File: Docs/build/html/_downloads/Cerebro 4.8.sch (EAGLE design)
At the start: 29 parts, among them IC1 OPA237N, T1 FJX3904TF

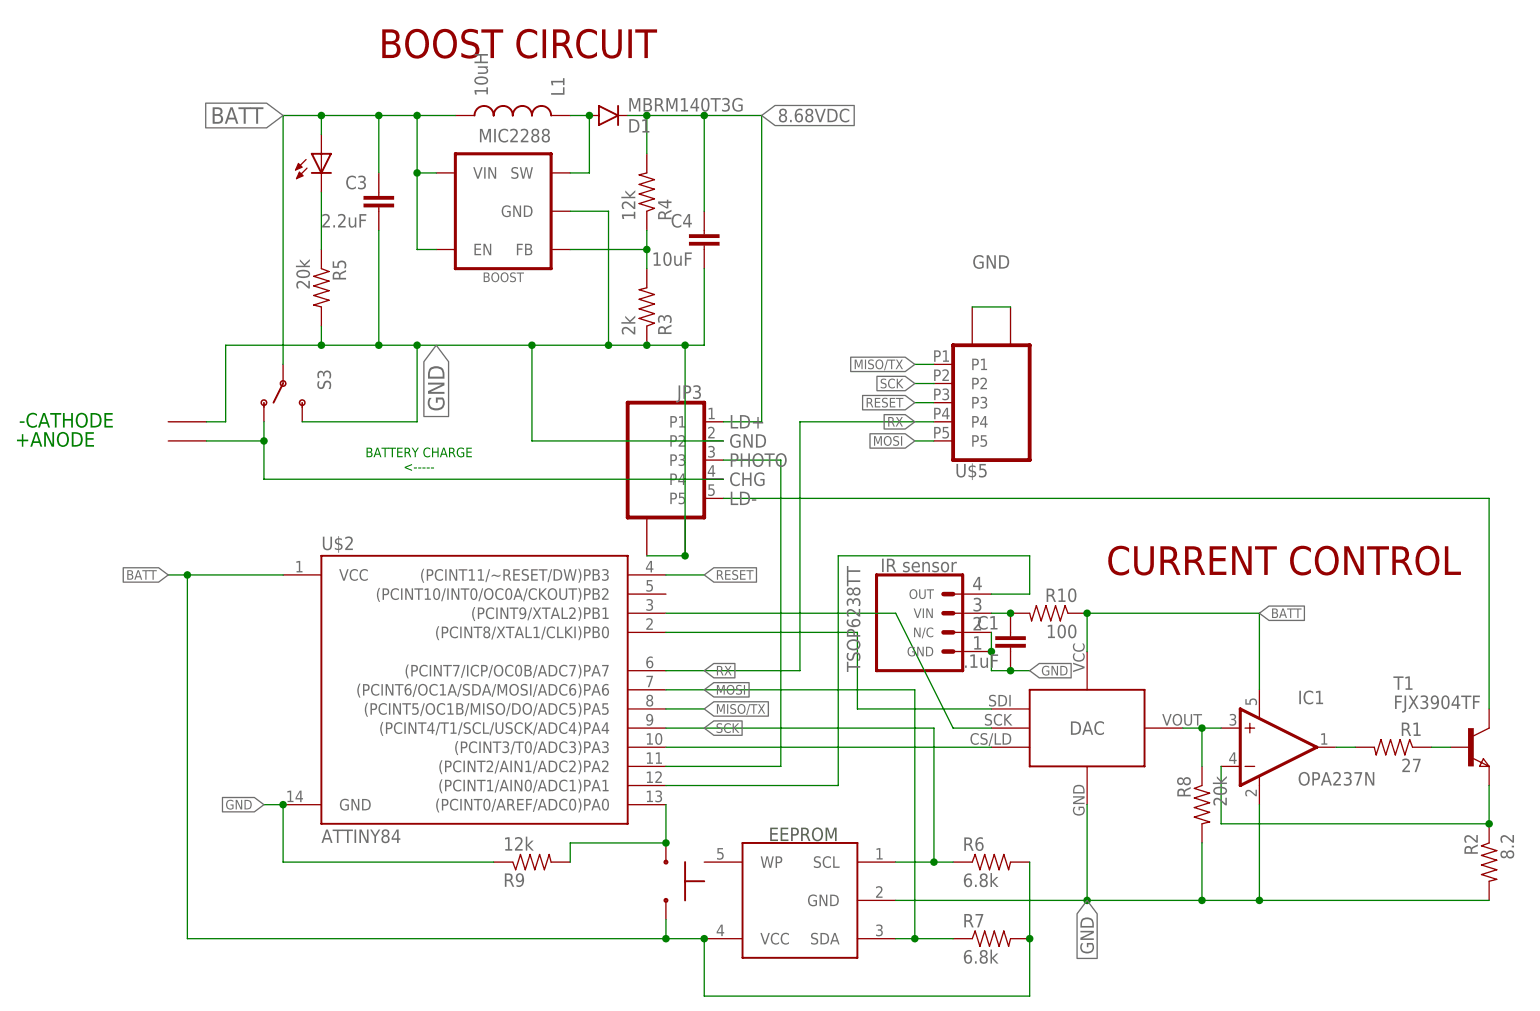
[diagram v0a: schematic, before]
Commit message: Cerebro PCB update to 4.8: - npn emitter resistor was 8.2ohm, now 6.8 ohm - removed push button resistor and changed to internal pullup resistor on MCU - switched to from 0805 to 0603 for all resistors and capacitors - switched to reinforced microUSB socket - enlarged ground pads on usb plug for stronger solder anchor - added indicator LED to pin 5 (PB2)
Updated cerebro.ino:
- pushbutton now gives a low signal when pressed.
- Arduino IDE update to 1.6.11 effected the delayMicroseconds(), thereby breaking the IR communication. Changed the irResolution to 4 in order to fix.

Updated docs to have Cerebro 4.8 files
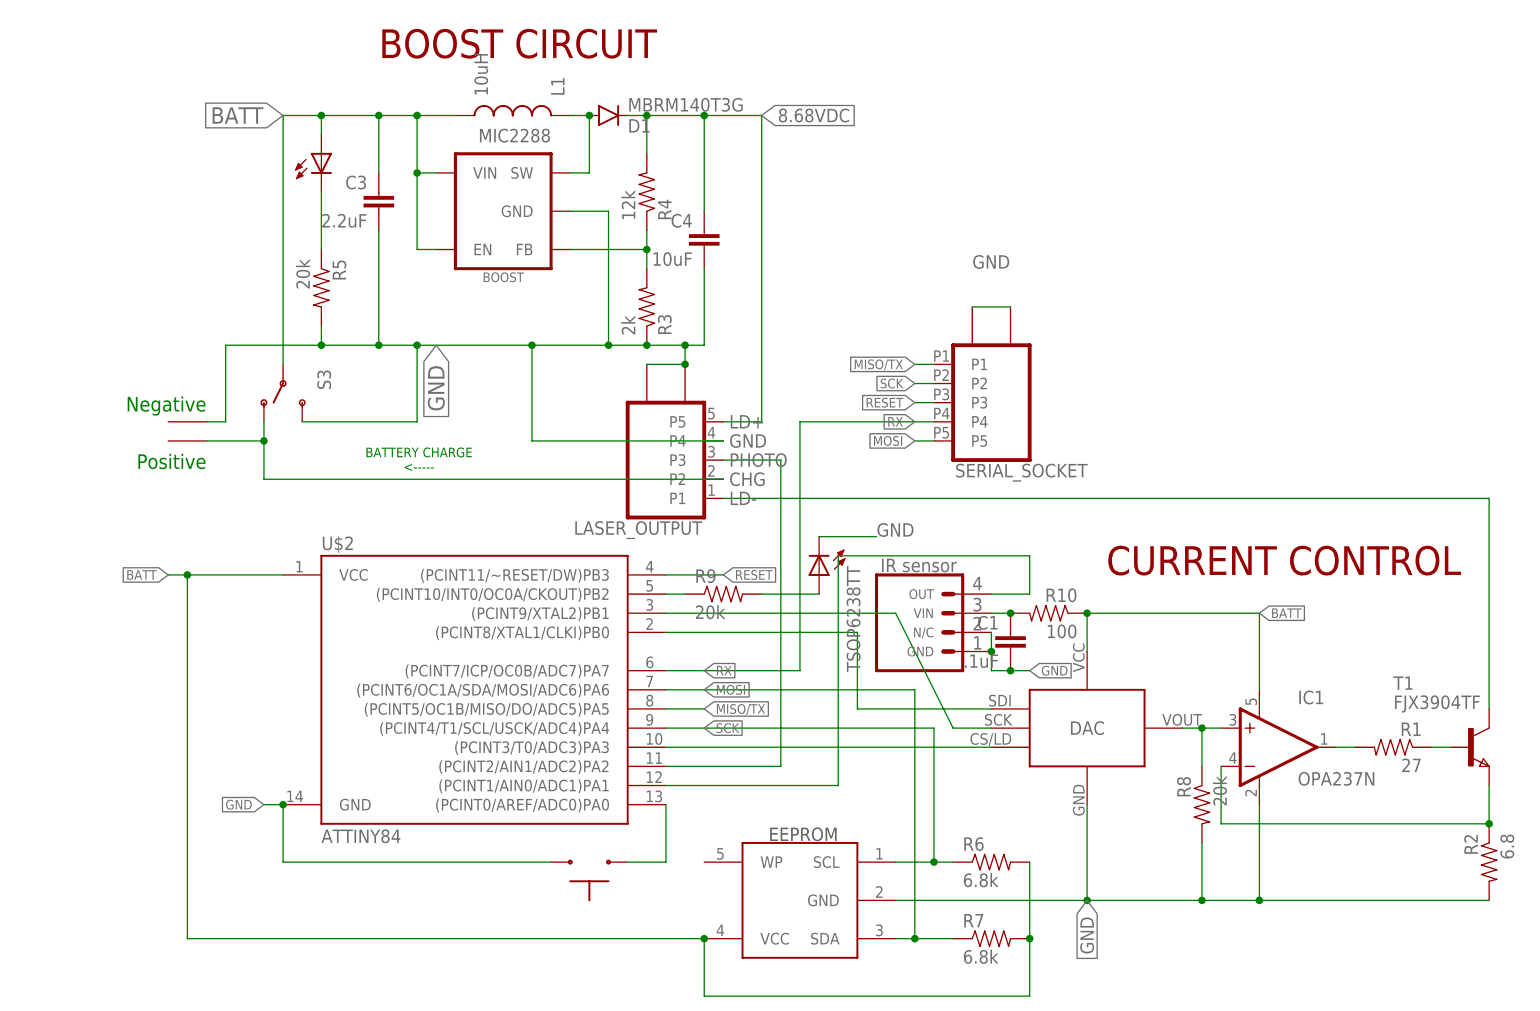
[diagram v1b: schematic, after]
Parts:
- removed U$5: USB_SOCKET_MICRO_VERTHORIZONTAL, Andy-library:USB_SOCKET_MICRO_VERTHORIZONTAL
- added INDICATOR_LED1: LED, led:LEDCHIP-LED0603
- added SERIAL_SOCKET: USB_SOCKET_MICRO_VERTREINFORCED, Andy-library:USB_SOCKET_MICRO_VERTREINFORCED
- R1, R3, R4, R6, R7, R8: device Andy-library:RESISTOR0805-RES -> Andy-library:RESISTOR0603-RES
- R2: value 8.2 -> 6.8; device Andy-library:RESISTOR0805-RES -> Andy-library:RESISTOR0603-RES
- R9: value 12k -> 20k; device Andy-library:RESISTOR0805-RES -> Andy-library:RESISTOR0603-RES
- renumbered JP3 to LASER_OUTPUT, U$7 to GROUND
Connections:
- new net N$17: LASER_OUTPUT.P1, T1.C
- new net N$18: INDICATOR_LED1.A, R9.2
- net 8.68VDC: now also LASER_OUTPUT.P5; no longer LASER_OUTPUT.P1
- net BATT: no longer U$3.2
- net GND: now also INDICATOR_LED1.C, LASER_OUTPUT.P4, SERIAL_SOCKET.P$1, SERIAL_SOCKET.P$2, U$3.2; no longer LASER_OUTPUT.P2, R9.1, U$5.P$1, U$5.P$2
- net MISO/TX: now also SERIAL_SOCKET.P1; no longer U$5.P1
- net MOSI: now also SERIAL_SOCKET.P5; no longer U$5.P5
- net N$13: now also R9.1, U$2.(PCINT10/INT0/OC0A/CKOUT)PB2; no longer LASER_OUTPUT.P5, T1.C
- net N$4: now also LASER_OUTPUT.P2; no longer LASER_OUTPUT.P4
- net N$7: no longer R9.2
- net RESET: now also SERIAL_SOCKET.P3; no longer U$5.P3
- net RX: now also SERIAL_SOCKET.P4; no longer U$5.P4
- net SCK: now also SERIAL_SOCKET.P2; no longer U$5.P2
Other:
- note added: "Negative"
- note added: "Positive"
- note removed: "+ANODE"
- note removed: "-CATHODE"
- moved on the sheet: R9
